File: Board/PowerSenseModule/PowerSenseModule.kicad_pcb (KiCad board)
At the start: 2 copper layers, 107.9 x 65 mm, 67 parts, among them J1 Conn_01x06_Male, J3 Programming Header, J4 Conn_01x02_Male, U1 TPS82150, U2 NCV2007x, U3 dsPIC33EV32GM102, U4 MCP2542FDxMF, Y1 25 MHz

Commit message: Generated gerber and fab files
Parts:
- added G1: LOGO, Logo:HKNZetaChi, F.Cu at (146.6, 113.2)
- added J2: ISENSE, Connector_PinHeader_2.54mm:PinHeader_1x01_P2.54mm_Vertical, F.Cu at (156.4, 97.4)
- added J5: VSENSE, Connector_PinHeader_2.54mm:PinHeader_1x01_P2.54mm_Vertical, F.Cu at (156.4, 101.8)
- H1, H2, H3, H4: value MountingHole_Pad -> (none)
- J1: value Conn_01x06_Male -> DT13-6P
- J4: value Conn_01x02_Male -> Board Interconnect
- JP1: value Jumper_NO_Small -> Program Enable
- R1: moved to F.Cu
- R6: footprint Capacitor_SMD:C_0603_1608Metric_Pad1.05x0.95mm_HandSolder -> Resistor_SMD:R_0603_1608Metric_Pad1.05x0.95mm_HandSolder
- moved R1 48.4 mm to (183.7, 73.6)
- moved H3 47.8 mm to (195.5, 117.0)
- moved H4 46.6 mm to (96.6, 117.0)
- moved C12 45.6 mm to (174.4, 102.9)
- moved C17 45.6 mm to (178.6, 99.0)
- moved C18 45.6 mm to (183.6, 99.0)
- moved C2 45.6 mm to (173.8, 69.5)
- moved C21 45.6 mm to (163.8, 76.2)
- moved C5 45.6 mm to (173.8, 73.3)
- moved C6 45.6 mm to (175.7, 73.3)
- moved C9 45.6 mm to (172.7, 99.3)
- moved D5 45.6 mm to (163.8, 72.0)
- moved D6 45.6 mm to (163.8, 74.3)
- moved J1 45.6 mm to (130.1, 87.4)
- moved J3 45.6 mm to (194.2, 98.0)
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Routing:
- net Net-(J5-Pad1): track 8.64 -> 29.7 mm, vias 0 -> 2
- net /CAN+: track 94.5 -> 100.0 mm
- net /CAN-: track 93.4 -> 98.9 mm
- net Net-(R1-Pad2): track 2.33 -> 7.53 mm, vias 1 -> 0
- net Net-(J2-Pad1): track 15.9 -> 18.5 mm
- net +5V: track 196.7 -> 196.1 mm
- net GND: vias 12 -> 22
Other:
- board size 107.9 x 65 mm -> 107.9 x 62.3 mm
- board text added: "DT13-6P has 1.9 mm hole diameter"
- board text added: "DT13-6P has height 36 mm"
- board text added: "Header connector has 1 mm hole diameter"
- board text added: "Header connectors are shorter than the DT13-6P"
- board text added: "Header connectors have 2.54 mm pitch"
- board text added: "Insert to prgm"
- board text added: "NOTES:"
- board text added: "Power Sensor"
- board text added: "Program Header"
- board text added: "REV 1.0"

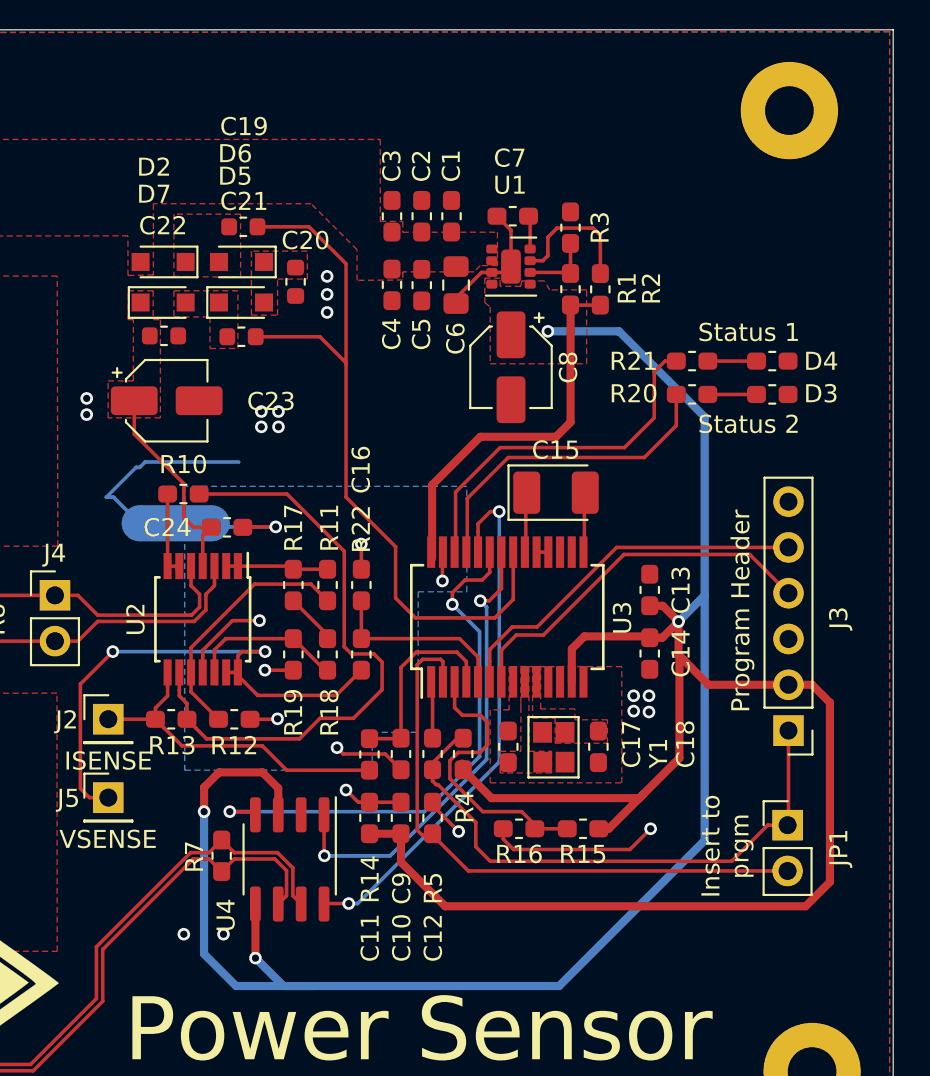
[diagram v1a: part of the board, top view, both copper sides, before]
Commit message: Updated BOM, schematic, PCB
- Using 3 pin jumper for program enable so that the jumper can be stored on the board
- Updated footprint for 4.7uF cap from electrolytic to smd 0805
- cleaned up some copper zones
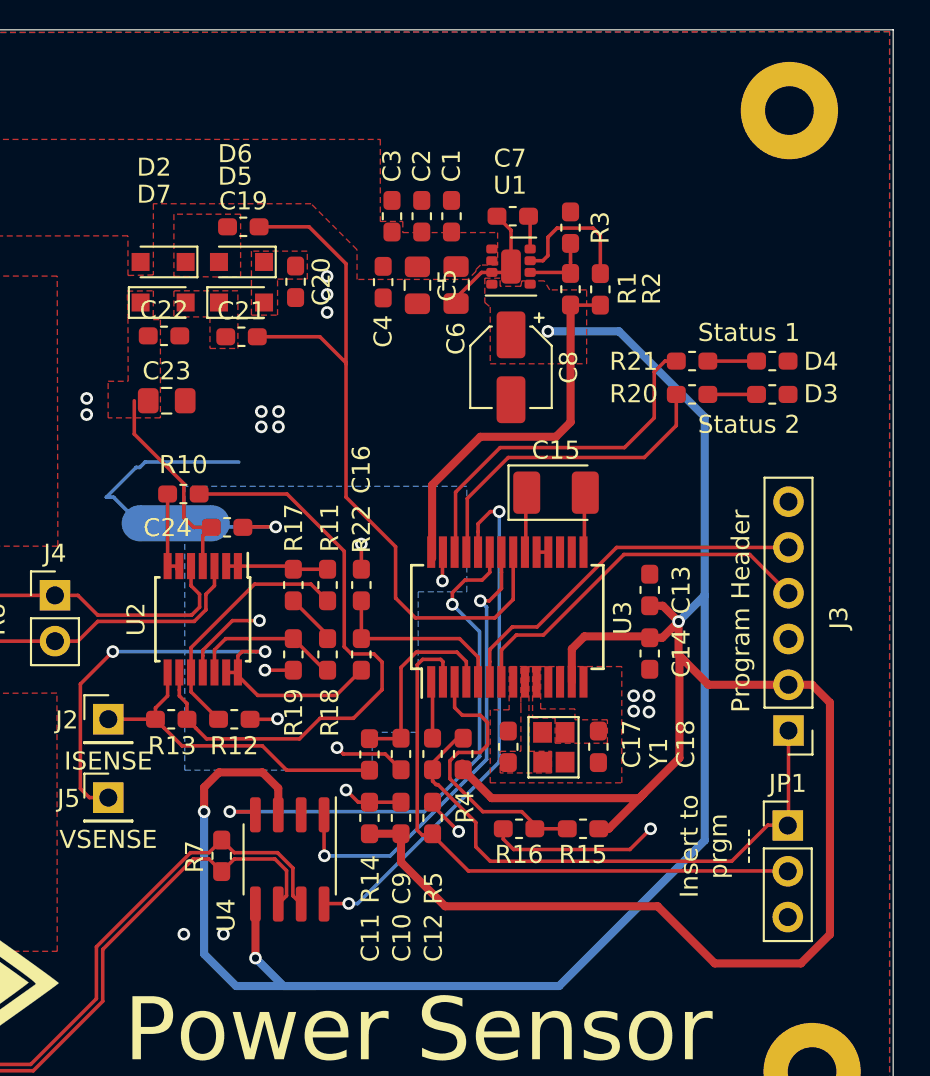
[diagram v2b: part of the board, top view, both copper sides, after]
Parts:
- C19, C20, C21, C22: footprint Capacitor_SMD:C_0603_1608Metric -> Capacitor_SMD:C_0603_1608Metric_Pad1.05x0.95mm_HandSolder
- C23: footprint Capacitor_SMD:CP_Elec_4x5.8 -> Capacitor_SMD:C_0805_2012Metric_Pad1.15x1.40mm_HandSolder
- C5: footprint Capacitor_SMD:C_0603_1608Metric_Pad1.05x0.95mm_HandSolder -> Capacitor_SMD:C_0805_2012Metric_Pad1.15x1.40mm_HandSolder
- C7: value 470p -> 470pF
- D2, D5, D6, D7: value D -> DPUMP
- D3: value LED -> GREEN_LED
- D4: value LED -> RED_LED
- JP1: value Program Enable -> PRGM_EN; footprint Connector_PinHeader_2.54mm:PinHeader_1x02_P2.54mm_Vertical -> Connector_PinHeader_2.54mm:PinHeader_1x03_P2.54mm_Vertical
- moved C4 0.51 mm to (171.7, 73.2)
- moved C5 0.24 mm to (173.6, 73.3)
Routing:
- net +5V: track 196.1 -> 200.5 mm
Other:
- board text added: "Insert to prgm ----"
- board text removed: "Insert to prgm"

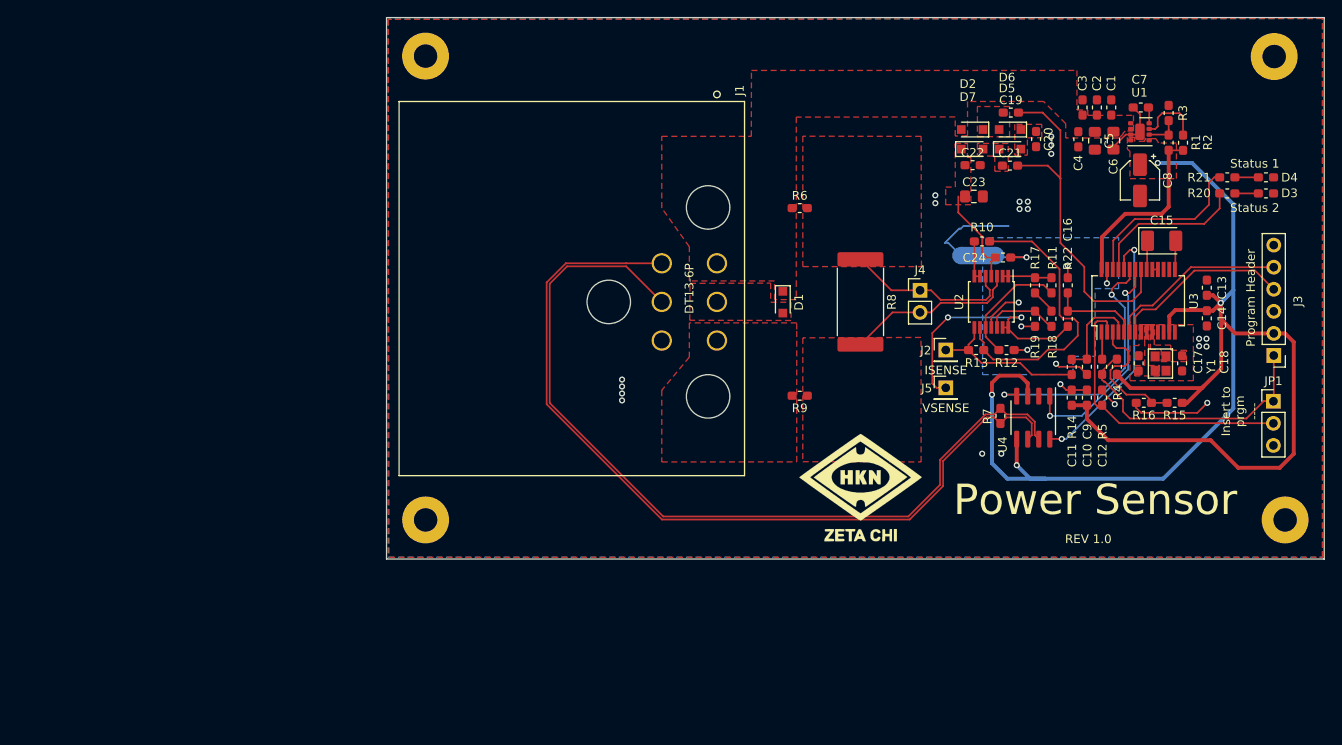
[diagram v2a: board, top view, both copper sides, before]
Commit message: PCB rev 1.10
>See GitHub issue for changes:
https://github.com/paulwood15/HKN-SAE-Project/issues/16

> Need to update BOM and do design review
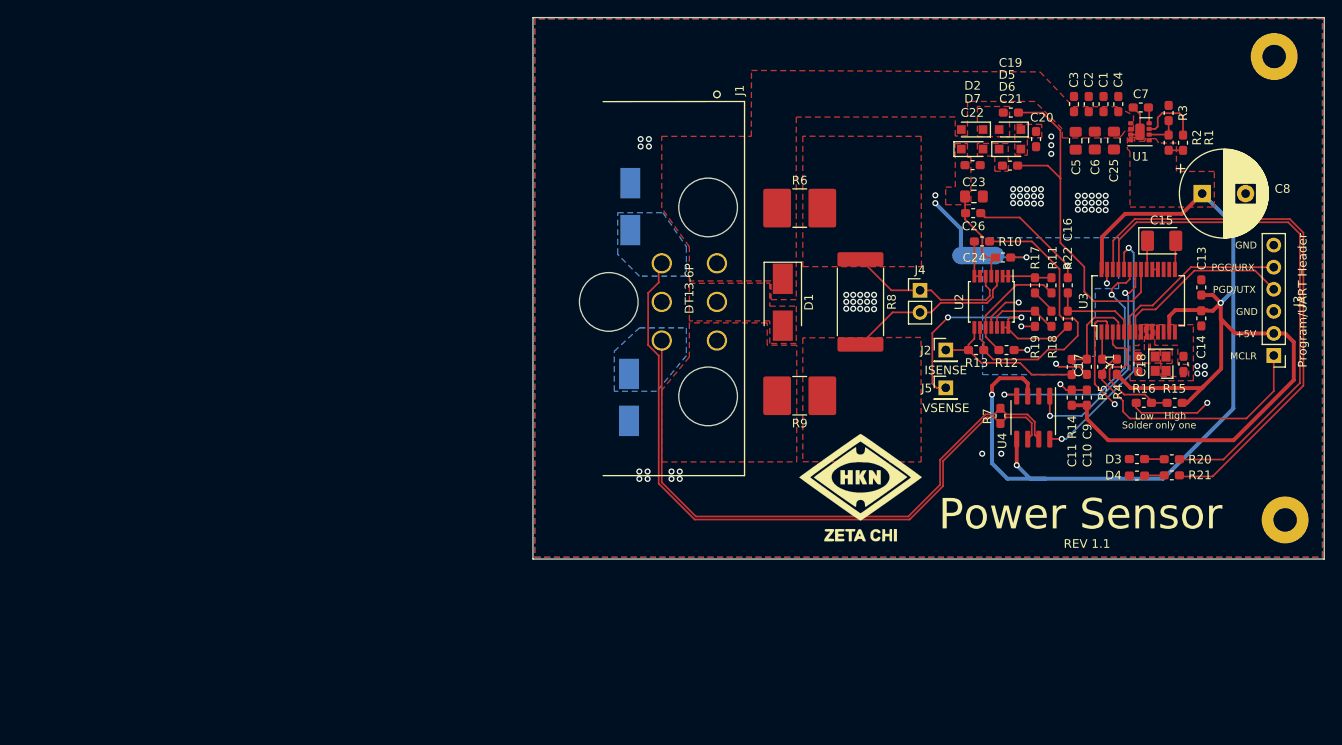
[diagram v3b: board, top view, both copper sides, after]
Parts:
- removed C12: 0.1uF, Capacitor_SMD:C_0603_1608Metric_Pad1.05x0.95mm_HandSolder
- removed the H1 at (96.5, 63.6)
- removed H4: , MountingHole:MountingHole_2.7mm_M2.5_Pad
- removed JP1: PRGM_EN, Connector_PinHeader_2.54mm:PinHeader_1x03_P2.54mm_Vertical
- added C25: 4.7uF, Capacitor_SMD:C_0805_2012Metric_Pad1.15x1.40mm_HandSolder, F.Cu at (175.8, 73.3)
- added C26: 0.1uF, Capacitor_SMD:C_0603_1608Metric_Pad1.05x0.95mm_HandSolder, F.Cu at (159.6, 81.7)
- added D8: SMBJ9.0CA-13-F, Diode_SMD:D_SMB_Handsoldering, B.Cu at (120.0, 102.9)
- added D9: SMBJ9.0CA-13-F, Diode_SMD:D_SMB_Handsoldering, B.Cu at (120.1, 80.9)
- C6: value 6.8uF -> 4.7uF
- C8: footprint Capacitor_SMD:CP_Elec_4x5.8 -> Capacitor_THT:CP_Radial_D10.0mm_P5.00mm
- D1: value SD05-7 -> SMBJ9.0CA-13-F; footprint Diode_SMD:D_SOD-323_HandSoldering -> Diode_SMD:D_SMB_Handsoldering
- J3: value Programming Header -> Program/UART Header
- R6, R9: footprint Resistor_SMD:R_0603_1608Metric_Pad1.05x0.95mm_HandSolder -> Resistor_SMD:R_2816_7142Metric_Pad3.20x4.45mm_HandSolder
- moved D4 37.4 mm to (178.4, 111.9), turned to 0 degrees
- moved R21 34.9 mm to (182.4, 111.8), turned to 0 degrees
- moved D3 34.0 mm to (178.4, 110.0), turned to 0 degrees
- moved R20 31.2 mm to (182.4, 110.0), turned to 0 degrees
- moved C8 7.32 mm to (185.9, 79.4), turned to 0 degrees
- moved C4 6.13 mm to (176.3, 69.1), turned to 90 degrees
- moved Y1 3.50 mm to (182.3, 100.3), turned to 90 degrees
- moved C5 2.20 mm to (171.4, 73.3)
- moved C6 2.15 mm to (173.6, 73.3)
- moved C3 1.06 mm to (171.2, 69.1)
- moved C2 1.02 mm to (172.9, 69.1)
- moved C1 0.97 mm to (174.6, 69.1)
- moved C13 0.64 mm to (185.8, 90.2)
- moved C14 0.64 mm to (185.8, 93.8)
- moved C18 0.17 mm to (183.8, 99.0), turned to 90 degrees
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- renumbered H2 to H1, H3 to H2
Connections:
- J1 pad 4: GND -> /CAN+
- J1 pad 5: /CAN+ -> GND
- U3 pad 2: Net-(C12-Pad1) -> GND
- Y1 pad 2: GND -> (no net)
- Y1 pad 4: (no net) -> GND
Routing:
- net /MCU and CAN/LED2: track 20.4 -> 63.5 mm
- net /MCU and CAN/LED1: track 18.6 -> 60.7 mm
- net Net-(C12-Pad1): track 34.5 -> 0.00 mm
- net /CAN+: track 100.0 -> 70.5 mm
- net /CAN-: track 98.9 -> 80.6 mm
- net +5V: track 200.5 -> 183.1 mm, vias 4 -> 3
- net GNDA: track 20.7 -> 33.2 mm
- net GND: track 36.6 -> 42.3 mm, vias 22 -> 71
- net /MCU and CAN/MCLR: track 31.7 -> 31.0 mm
- added copper zone on B.Cu, net /CAN+
- added copper zone on B.Cu, net /CAN-
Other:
- board size 107.9 x 62.3 mm -> 91.1 x 62.3 mm
- board text added: "+12V"
- board text added: "+5V"
- board text added: "CAN+"
- board text added: "CAN-"
- board text added: "GND"
- board text added: "High"
- board text added: "Low"
- board text added: "MCLR"
- board text added: "MEAS_OUT"
- board text added: "PGC/URX"
- board text added: "PGD/UTX"
- board text added: "Program/UART Header"
- board text added: "REV 1.1"
- board text added: "Solder only one"
- board text removed: "Insert to prgm ----"
- board text removed: "Program Header"
- board text removed: "REV 1.0"
- board text removed: "Status 1"
- board text removed: "Status 2"

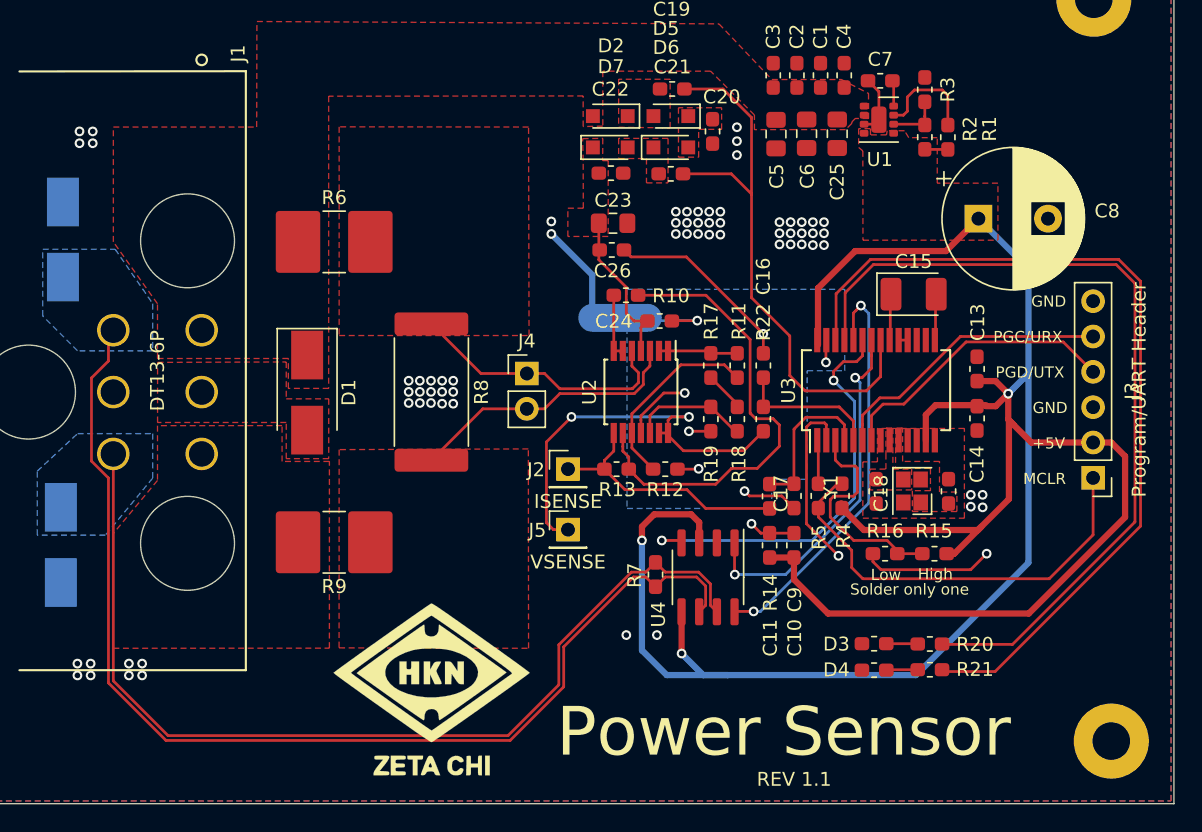
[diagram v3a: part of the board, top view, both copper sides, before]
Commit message: PCB rev 1.11
- replaced 47 uF electrolytic with 3 22 uF because it's cheaper and to account for derating
- updated BOM
- added inventory
 > need to merge two excel sheets (inventory and BOM) 
- added TVS zener diodes for CAN+ and CAN-
- updated input protection diode with the one used by CAN+ and CAN-
- rerouted CAN+ and CAN- for pinout change in main connector (DT13-6P)
- changed pinout of the DT13-6P so that the protection diode copper fills would be symmetric 
- added 0.1 uF decoupling cap to op amp VDD input
- added danger high voltage graphic copper and mask
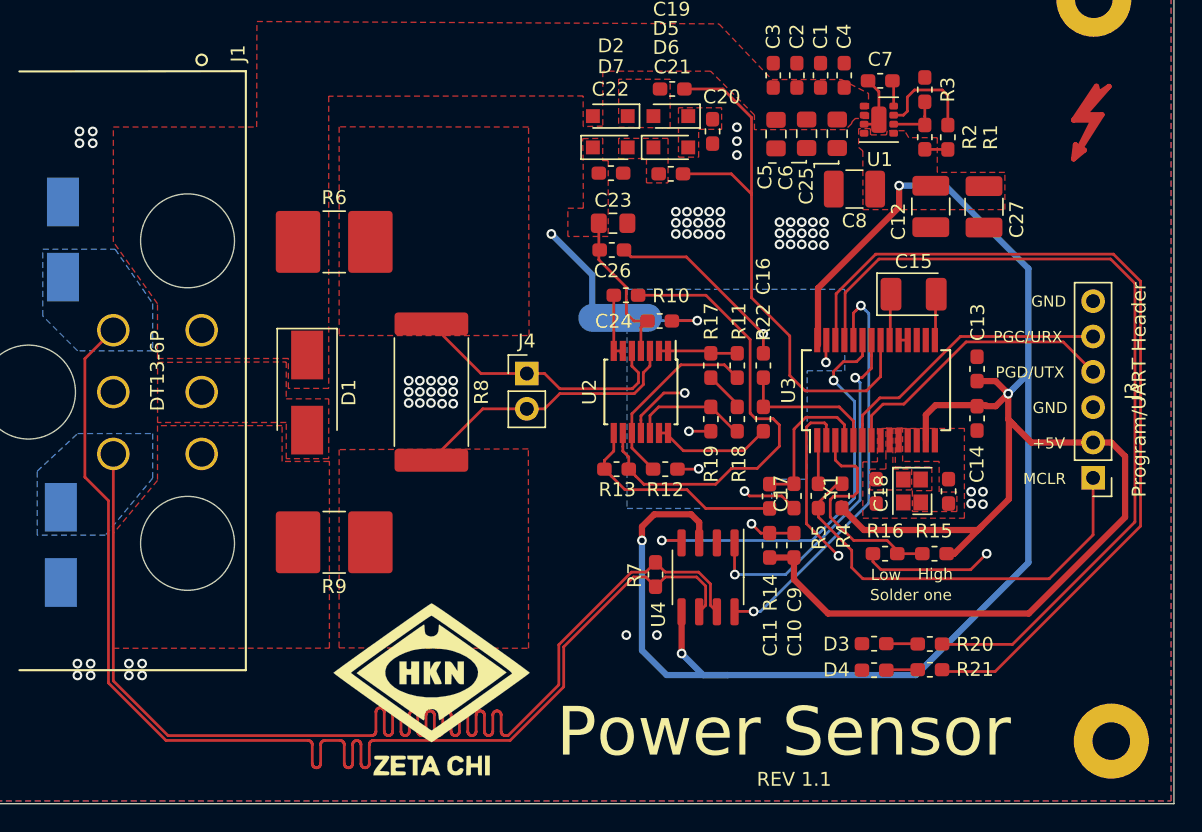
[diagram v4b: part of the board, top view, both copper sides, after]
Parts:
- removed J2: ISENSE, Connector_PinHeader_2.54mm:PinHeader_1x01_P2.54mm_Vertical
- removed J5: VSENSE, Connector_PinHeader_2.54mm:PinHeader_1x01_P2.54mm_Vertical
- added C12: 22uF, Capacitor_SMD:C_1210_3225Metric_Pad1.42x2.65mm_HandSolder, F.Cu at (182.5, 78.5)
- added C27: 22uF, Capacitor_SMD:C_1210_3225Metric_Pad1.42x2.65mm_HandSolder, F.Cu at (186.3, 78.6)
- added Danger: Symbol_Highvoltage_Type1_CopperTop_Small, Symbol:Symbol_Highvoltage_Type1_CopperTop_Small, F.Cu at (193.1, 73.1)
- C8: value 47uF -> 22uF; footprint Capacitor_THT:CP_Radial_D10.0mm_P5.00mm -> Capacitor_SMD:C_1210_3225Metric_Pad1.42x2.65mm_HandSolder
- J3: value Program/UART Header -> Programming Header
- moved C8 9.16 mm to (177.0, 77.3), turned to 180 degrees
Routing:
- net /CAN+: track 70.5 -> 95.3 mm
- net Net-(R22-Pad2): track 29.7 -> 8.64 mm, vias 2 -> 0
- net /CAN-: track 80.6 -> 91.2 mm
- net +5V: track 183.1 -> 186.0 mm, vias 3 -> 4
- net Net-(R13-Pad1): track 18.5 -> 15.9 mm
- net GND: vias 71 -> 70
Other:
- board text added: "Solder one"
- board text removed: "Solder only one"
